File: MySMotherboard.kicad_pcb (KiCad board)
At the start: 2 copper layers, 26.2 x 45.1 mm, 45 parts, among them IC1 APE8865Y5-30-HF-3, IC2 AT25DF512C-SSHN-B, IC3 ATSHA204A, IC4 MCP1640CT-I/CHY, IC5 ATMEGA328P-AU, Q2 FA-128

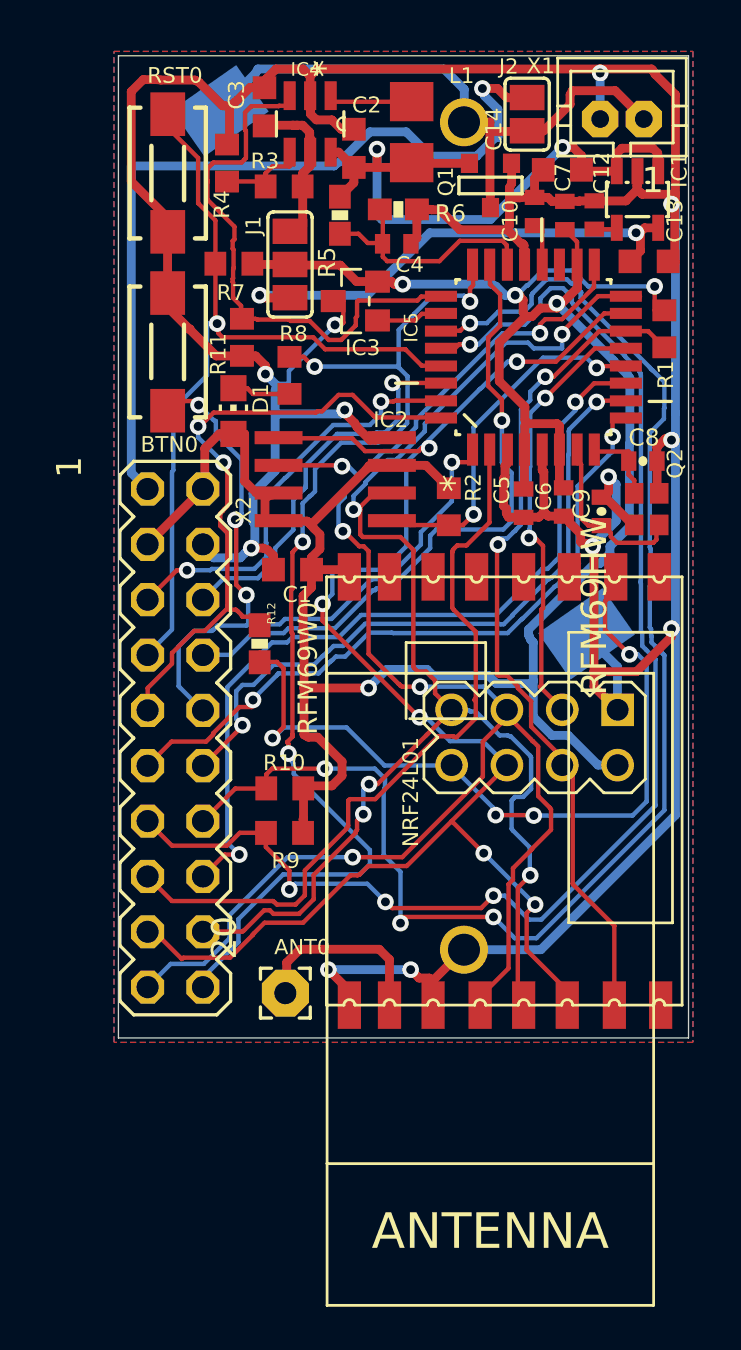
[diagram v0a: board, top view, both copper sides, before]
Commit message: refactor schematic to use native KiCad symbols and footprints
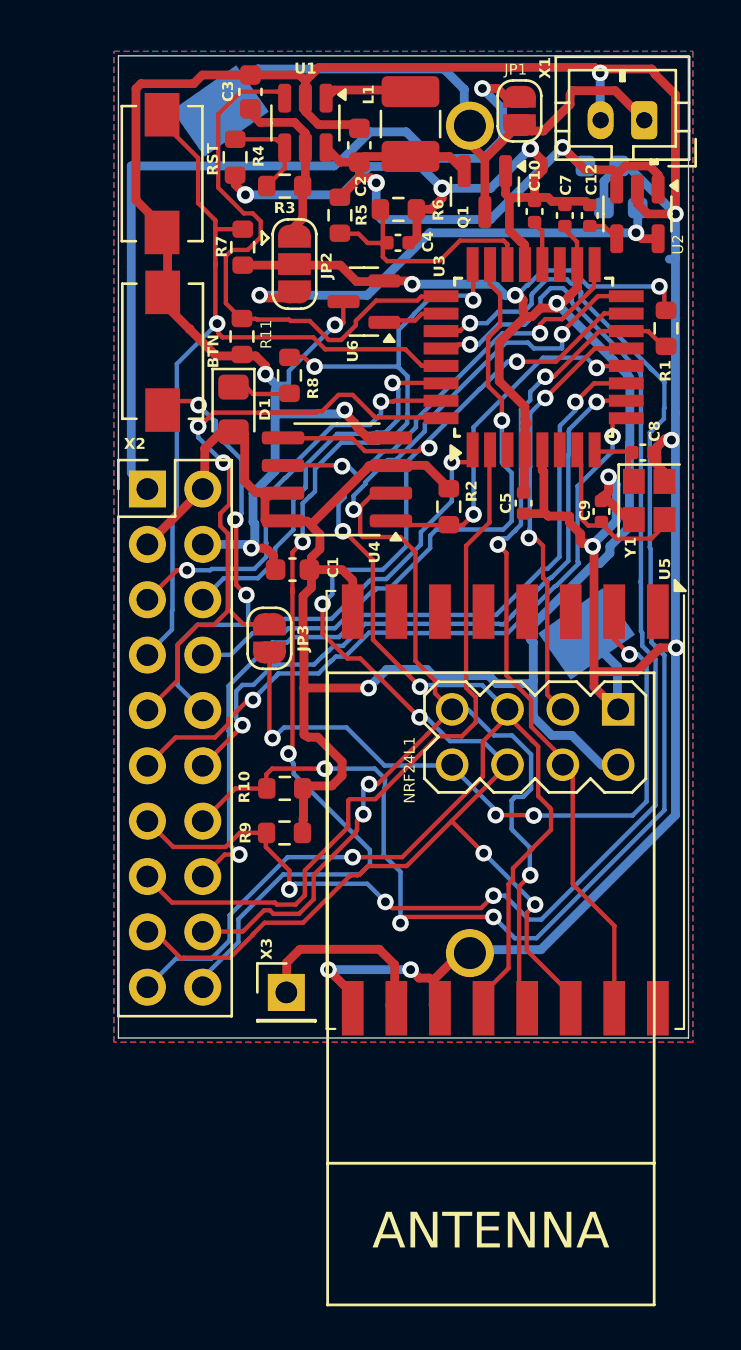
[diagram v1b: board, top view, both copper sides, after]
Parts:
- removed ANT0: WIREPAD2,15/1,0, MySMotherboard:2,15_1,0
- removed BTN0, RST0: DTSM-3, MySMotherboard:DTSM-3
- removed C6: 100n, MySMotherboard:C0402
- removed CR123A0: BAT_PACKCR123A, MySMotherboard:BH123A
- removed CR2032: , MySMotherboard:79527141
- removed IC1: APE8865Y5-30-HF-3, MySMotherboard:SOT25
- removed IC2: AT25DF512C-SSHN-B, MySMotherboard:SO-08
- removed IC3: ATSHA204A, MySMotherboard:SOT23
- removed IC4: MCP1640CT-I/CHY, MySMotherboard:SOT95P270X145-6N
- removed IC5: ATMEGA328P-AU, MySMotherboard:QFP80P900X900X120-32N
- removed J1: , MySMotherboard:SJ_2
- removed J2: , MySMotherboard:SJ
- removed NRF24L01: WIRELESS-NRF24L01, MySMotherboard:WIRELESS-NRF24L01
- removed Q2: FA-128, MySMotherboard:FA-128
- removed R12: 0, MySMotherboard:0603-RES
- removed RFM69W0: RFM69HW, MySMotherboard:RFM
- added BT1: CR2032, Battery:BatteryHolder_Keystone_1060_1x2032, B.Cu at (148.5, 97.0)
- added BT2: CR123A, MySMotherboard:BH123A, B.Cu at (151.6, 104.7)
- added JP1: ~, Jumper:SolderJumper-2_P1.3mm_Open_RoundedPad1.0x1.5mm, F.Cu at (153.8, 85.0)
- added JP2: ~, Jumper:SolderJumper-3_P1.3mm_Open_RoundedPad1.0x1.5mm, F.Cu at (143.5, 92.0)
- added JP3: ~, Jumper:SolderJumper-2_P1.3mm_Open_RoundedPad1.0x1.5mm, F.Cu at (142.3, 109.2)
- added NRF24L1: WIRELESS-NRF24L01, MySMotherboard:WIRELESS-NRF24L01, F.Cu at (152.0, 125.2)
- added SW1: RST, Button_Switch_SMD:SW_SPST_EVQPE1, F.Cu at (137.4, 87.9)
- added SW2: BTN, Button_Switch_SMD:SW_SPST_EVQPE1, F.Cu at (137.4, 96.0)
- added U1: MCP1640Cx-xCHY, Package_TO_SOT_SMD:SOT-23-6, F.Cu at (144.0, 85.5)
- added U2: APE8865Y5-30-HF-3, Package_TO_SOT_SMD:SOT-23-5, F.Cu at (159.2, 89.7)
- added U3: ATmega328PB-A, Package_QFP:TQFP-32_7x7mm_P0.8mm, F.Cu at (154.5, 96.3)
- added U4: AT25xxx, Package_SO:SOIC-8_3.9x4.9mm_P1.27mm, F.Cu at (145.4, 101.9)
- added U5: RFM69HW, RF_Module:HOPERF_RFM69HW, F.Cu at (153.2, 117.1)
- added U6: ATSHA204A, Package_TO_SOT_SMD:SOT-23, F.Cu at (146.7, 93.8)
- added X3: ANT, Connector_PinHeader_2.54mm:PinHeader_1x01_P2.54mm_Vertical, F.Cu at (143.1, 125.5)
- added Y1: 16M, Crystal:Crystal_SMD_2520-4Pin_2.5x2.0mm, F.Cu at (159.8, 102.9)
- C1, C3: footprint MySMotherboard:C0603K -> Capacitor_SMD:C_0603_1608Metric
- C10, C4, C5, C7: footprint MySMotherboard:C0402 -> Capacitor_SMD:C_0402_1005Metric
- C12: value 10n -> 100n; footprint MySMotherboard:C0402 -> Capacitor_SMD:C_0402_1005Metric
- C13: footprint MySMotherboard:C0603K -> Capacitor_SMD:C_0603_1608Metric; moved to B.Cu
- C14: value 10u -> 10u/16V; footprint MySMotherboard:C0603K -> Capacitor_SMD:C_0603_1608Metric; moved to B.Cu
- C2: value 4.7u -> 10u; footprint MySMotherboard:C0603K -> Capacitor_SMD:C_0603_1608Metric
- C8, C9: footprint MySMotherboard:0402-CAP -> Capacitor_SMD:C_0402_1005Metric
- D1: value (none) -> LED; footprint MySMotherboard:CHIP-LED0805 -> LED_SMD:LED_0805_2012Metric_Pad1.15x1.40mm_HandSolder
- L1: footprint MySMotherboard:L3225P -> Inductor_SMD:L_1210_3225Metric_Pad1.42x2.65mm_HandSolder
- Q1: value (none) -> ~; footprint MySMotherboard:SOT-23 -> Package_TO_SOT_SMD:SOT-23
- R1, R10, R11, R2, R3, R4, R7, R8, R9: footprint MySMotherboard:R0603 -> Resistor_SMD:R_0603_1608Metric
- R5, R6: footprint MySMotherboard:0603-RES -> Resistor_SMD:R_0603_1608Metric
- X1: value (none) -> ~; footprint MySMotherboard:JST-PH2 -> Connector_JST:JST_PH_B2B-PH-K_1x02_P2.00mm_Vertical
- X2: value (none) -> MySX 2.5; footprint MySMotherboard:MA10-2 -> Connector_PinHeader_2.54mm:PinHeader_2x10_P2.54mm_Vertical
- moved X2 11.5 mm to (136.8, 102.3), turned to 0 degrees
- moved C13 2.78 mm to (158.5, 89.5), turned to 180 degrees
- moved C14 1.84 mm to (157.6, 87.5), turned to 0 degrees
- moved X1 1.02 mm to (159.6, 85.4), turned to 180 degrees
- moved C3 0.94 mm to (141.5, 84.1)
- moved R7 0.86 mm to (141.1, 91.2), turned to 90 degrees
- moved R4 0.46 mm to (140.8, 87.1)
- moved C8 0.39 mm to (159.5, 100.7)
- moved L1 0.37 mm to (148.8, 85.6), turned to 90 degrees
- moved Q1 0.36 mm to (152.2, 88.7), turned to -90 degrees
- moved C2 0.29 mm to (146.5, 86.6)
- moved C12 0.21 mm to (157.1, 89.8), turned to 90 degrees
- moved R1 0.08 mm to (160.6, 95.0)
- moved C4 0.07 mm to (148.2, 91.0)
- moved D1 0.07 mm to (140.7, 98.7), turned to -90 degrees
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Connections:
- C12 pad 1: GND -> Net-(U2-BYP)
- C12 pad 2: N$8 -> GND
- C5 pad 1: GND -> VCC
- C5 pad 2: VCC -> GND
- C7 pad 1: GND -> VCC
- C7 pad 2: VCC -> GND
- C9 pad 1: GND -> Net-(U3-XTAL1/PB6)
- C9 pad 2: N$6 -> GND
- L1 pad 1: N$4 -> VBAT
- L1 pad 2: VBAT -> /SW_L
- Q1 pad 1: N$7 -> GND
- Q1 pad 3: GND -> /VIN
- R2 pad 1: D8 -> VCC
- R2 pad 2: VCC -> D8
- R3 pad 1: N$1 -> VBOOST
- R3 pad 2: VBOOST -> Net-(U1-V_{FB})
- R4 pad 1: GND -> Net-(U1-V_{FB})
- R4 pad 2: N$1 -> GND
- R5 pad 1: A7 -> VBAT
- R5 pad 2: VBAT -> A7
- R6 pad 1: GND -> A7
- R6 pad 2: A7 -> GND
- R8 pad 1: N$10 -> Net-(D1-K)
- R9 pad 1: A5 -> VCC
- R9 pad 2: VCC -> A5
- X1 pad 1: N$7 -> /VIN
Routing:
- net N$9: track 36.7 -> 0.00 mm, vias 4 -> 0
- net Net-(JP3-B): track 0.00 -> 34.0 mm, vias 0 -> 4
- net /VIN: track 0.00 -> 28.1 mm
- net N$7: track 27.8 -> 0.00 mm
- net Net-(U5-ANA): track 0.00 -> 8.88 mm
- net N$5: track 8.68 -> 0.00 mm
- net N$6: track 8.18 -> 0.00 mm
- net Net-(U3-XTAL1/PB6): track 0.00 -> 8.10 mm
- net GND: track 196.6 -> 203.0 mm, vias 12 -> 15
- net N$1: track 4.84 -> 0.00 mm
- net Net-(U1-V_{FB}): track 0.00 -> 4.54 mm
- net N$4: track 4.30 -> 0.00 mm
- net /SW_L: track 0.00 -> 4.08 mm
- net VCC: track 125.5 -> 121.6 mm
- net Net-(D1-K): track 0.00 -> 2.69 mm
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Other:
- board text added: "MySMotherboard v1.4"
- board text removed: "MySMotherboard v1.3"

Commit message: replace NRF24L01 with RS485 inteface
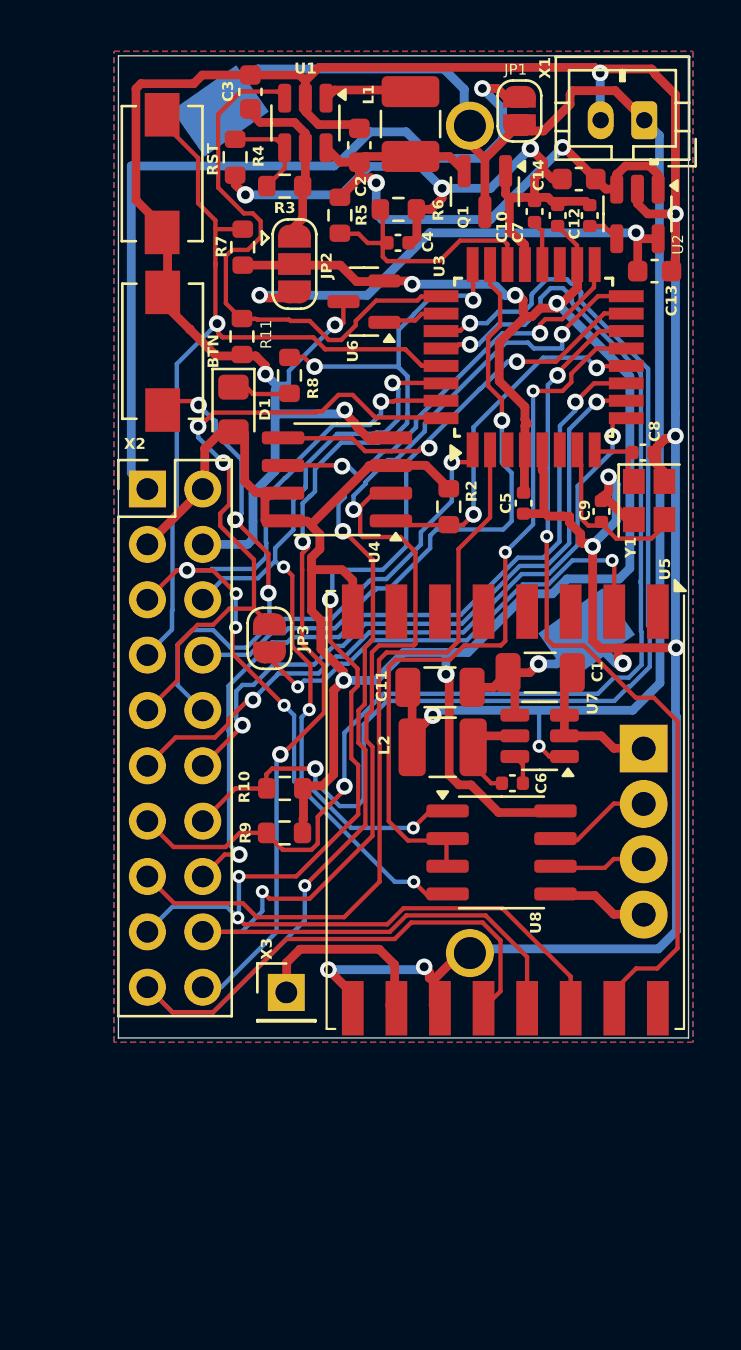
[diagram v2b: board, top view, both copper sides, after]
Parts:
- removed NRF24L1: WIRELESS-NRF24L01, MySMotherboard:WIRELESS-NRF24L01
- removed R1: 1M, Resistor_SMD:R_0603_1608Metric
- added C11: 22u, Capacitor_SMD:C_1206_3216Metric, F.Cu at (150.2, 111.5)
- added C6: 100n, Capacitor_SMD:C_0402_1005Metric, F.Cu at (153.5, 115.8)
- added L2: 4.7u, Inductor_SMD:L_1210_3225Metric, F.Cu at (150.3, 114.2)
- added U7: AP63205WU, Package_TO_SOT_SMD:TSOT-23-6, F.Cu at (154.8, 113.7)
- added U8: MAX3485, Package_SO:SOIC-8_3.9x4.9mm_P1.27mm, F.Cu at (153.0, 119.0)
- added X4: ~, TerminalBlock_Phoenix:TerminalBlock_Phoenix_MPT-0,5-4-2.54_1x04_P2.54mm_Horizontal, B.Cu at (159.5, 114.3)
- C1: value 10u -> 10u/50V; footprint Capacitor_SMD:C_0603_1608Metric -> Capacitor_SMD:C_1206_3216Metric
- C13, C14: moved to F.Cu
- moved C1 12.3 mm to (154.8, 110.8), turned to 180 degrees
- moved C13 3.29 mm to (160.0, 92.3), turned to 0 degrees
- moved C14 1.23 mm to (156.6, 88.1), turned to 180 degrees
- moved C7 0.33 mm to (155.6, 89.8)
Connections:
- net /VIN renamed VIN
- net VBAT renamed VINT
- C1 pad 1: GND -> +24V
- C1 pad 2: VCC -> GND
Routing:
- net VIN: track 28.1 -> 73.0 mm, vias 0 -> 2
- net TX: track 19.4 -> 41.1 mm, vias 2 -> 6
- net RX: track 18.2 -> 37.0 mm, vias 1 -> 4
- net D9: track 20.1 -> 34.5 mm
- net Net-(JP3-B): track 34.0 -> 21.3 mm, vias 4 -> 2
- net A4: track 66.0 -> 54.1 mm, vias 4 -> 2
- net VCC: track 121.6 -> 114.1 mm
- net +24V: track 0.00 -> 6.93 mm
- net GND: track 203.0 -> 209.8 mm, vias 15 -> 16
- net A5: track 62.0 -> 55.4 mm, vias 4 -> 2
- net Net-(U8-B): track 0.00 -> 4.80 mm
- net /SW_L2: track 0.00 -> 4.76 mm
- net Net-(U8-A): track 0.00 -> 4.28 mm
- net A1: track 52.0 -> 48.5 mm
- net MOSI: track 74.5 -> 71.9 mm, vias 6 -> 5
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
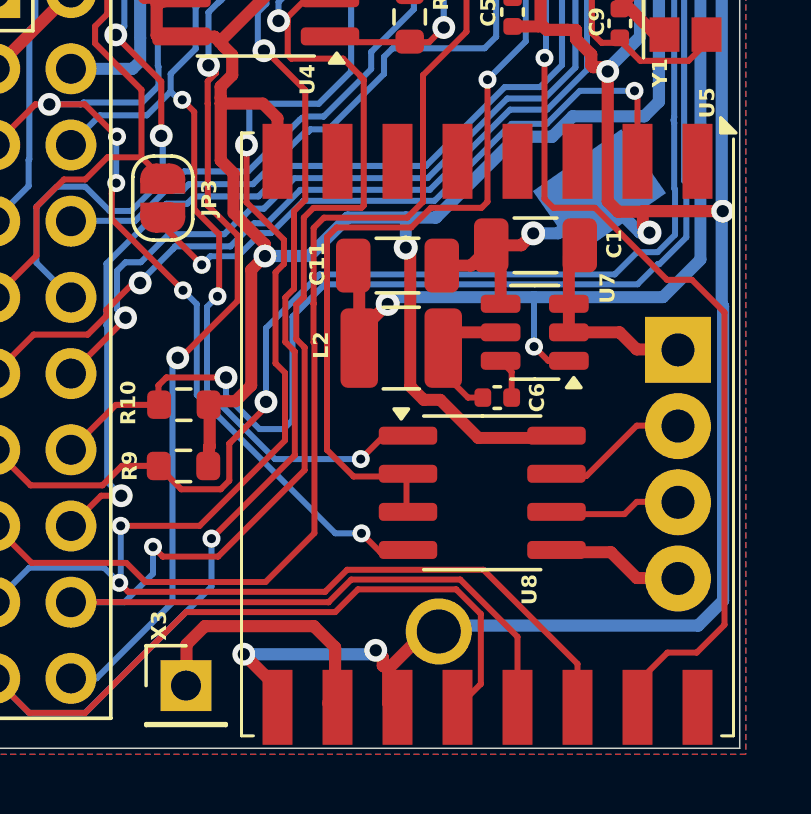
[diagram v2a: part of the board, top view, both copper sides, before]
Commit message: update PCB with latest changes
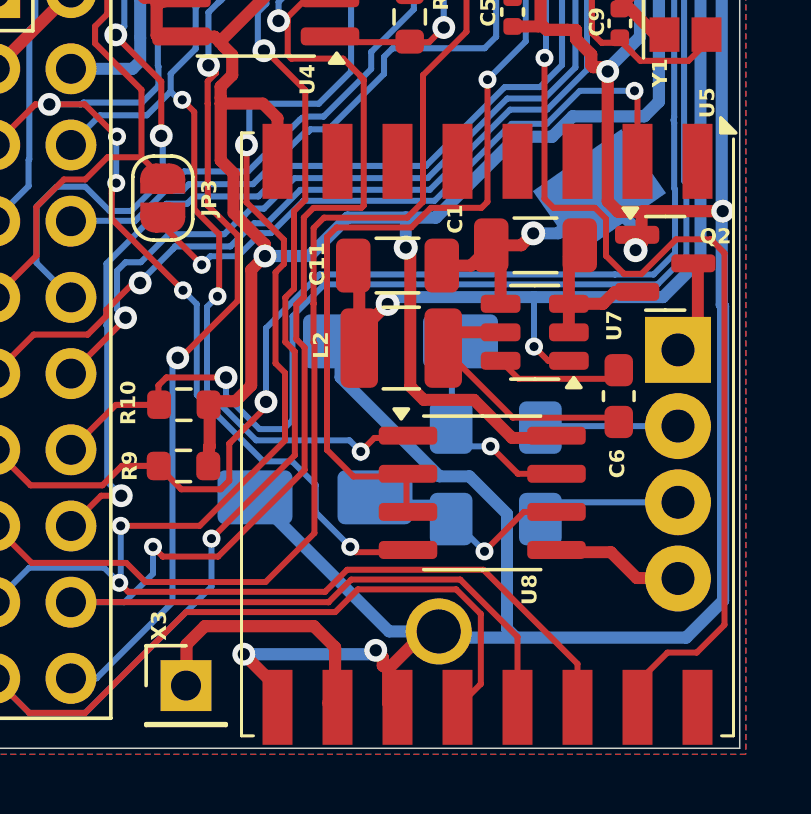
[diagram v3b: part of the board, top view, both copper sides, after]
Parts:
- added D2: SMAJ11CA, Diode_SMD:D_SMA, B.Cu at (147.4, 119.2)
- added D3: SMAJ11CA, Diode_SMD:D_SMA, B.Cu at (150.3, 114.0)
- added F1: Polyfuse, Fuse:Fuse_1206_3216Metric_Pad1.42x1.75mm_HandSolder, B.Cu at (153.4, 116.8)
- added F2: Polyfuse, Fuse:Fuse_1206_3216Metric_Pad1.42x1.75mm_HandSolder, B.Cu at (153.4, 119.9)
- added Q2: ~, Package_TO_SOT_SMD:SOT-23, F.Cu at (159.1, 111.4)
- C6: value 100n -> 100n/50V; footprint Capacitor_SMD:C_0402_1005Metric -> Capacitor_SMD:C_0603_1608Metric_Pad1.08x0.95mm_HandSolder
- U8: value MAX3485 -> SP3481EN
- moved C6 4.05 mm to (157.6, 115.8), turned to -90 degrees
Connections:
- net /SW_L2 renamed Net-(U7-SW)
- U8 pad 6: Net-(U8-A) -> Net-(D2-A2)
- U8 pad 7: Net-(U8-B) -> Net-(D3-A2)
- X4 pad 1: +24V -> Net-(Q2-D)
- X4 pad 2: Net-(U8-B) -> Net-(X4-Pin_2)
- X4 pad 3: Net-(U8-A) -> Net-(X4-Pin_3)
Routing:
- net GND: track 209.8 -> 231.8 mm
- net Net-(D2-A2): track 0.00 -> 8.13 mm, vias 0 -> 1
- net Net-(D3-A2): track 0.00 -> 7.12 mm, vias 0 -> 1
- net Net-(U8-B): track 4.80 -> 0.00 mm
- net Net-(X4-Pin_3): track 0.00 -> 4.59 mm
- net Net-(X4-Pin_2): track 0.00 -> 4.58 mm
- net Net-(U7-SW): track 4.76 -> 9.14 mm
- net Net-(U8-A): track 4.28 -> 0.00 mm
- net Net-(Q2-D): track 0.00 -> 3.15 mm
- net Net-(U7-BST): track 1.38 -> 4.31 mm
- net D10: track 38.8 -> 41.6 mm
- net +24V: track 6.93 -> 5.64 mm
- net TX: track 41.1 -> 41.7 mm
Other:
- board text removed: "Licensed under CERN OHL v.1.2"
